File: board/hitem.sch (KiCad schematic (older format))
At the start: 44 parts, among them J1 Female, 0.1\", 1x10, J2 Female, 0.1\", 1x10, J3 Header, .100\", J4 CONN_01X03, J5 Header, .100\", J6 CONN_01X01, J7 CONN_01X01, Q1 BSS214N, Q2 BSS214N, Q3 BSS214N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

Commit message: Fix incorrect footprint for U2
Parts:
- U2: footprint hitem:XC6221 -> hitem:SSOT-24
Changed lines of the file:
@@
 $EndComp
 $Comp
-L GND #PWR16
+L GND #PWR01
 U 1 1 56BBA380
 P 9350 4450
-F 0 "#PWR16" H 9350 4200 50  0001 C CNN
+F 0 "#PWR01" H 9350 4200 50  0001 C CNN
 F 1 "GND" H 9350 4300 50  0000 C CNN
 F 2 "" H 9350 4450 50  0000 C CNN
@@
 $EndComp
 $Comp
-L +BATT #PWR17
+L +BATT #PWR02
 U 1 1 56BD2B63
 P 9600 3500
-F 0 "#PWR17" H 9600 3350 50  0001 C CNN
+F 0 "#PWR02" H 9600 3350 50  0001 C CNN
 F 1 "+BATT" H 9600 3640 50  0000 C CNN
 F 2 "" H 9600 3500 50  0000 C CNN
@@
 $EndComp
 $Comp
-L GND #PWR2
+L GND #PWR03
 U 1 1 56BDEC0D
 P 1300 2450
-F 0 "#PWR2" H 1300 2200 50  0001 C CNN
+F 0 "#PWR03" H 1300 2200 50  0001 C CNN
 F 1 "GND" H 1300 2300 50  0000 C CNN
 F 2 "" H 1300 2450 50  0000 C CNN
@@
 $EndComp
 $Comp
-L +BATT #PWR12
+L +BATT #PWR04
 U 1 1 56BE7511
 P 6550 6350
-F 0 "#PWR12" H 6550 6200 50  0001 C CNN
+F 0 "#PWR04" H 6550 6200 50  0001 C CNN
 F 1 "+BATT" H 6550 6490 50  0000 C CNN
 F 2 "" H 6550 6350 50  0000 C CNN
@@
 Accelerometer
 $Comp
-L +BATT #PWR15
+L +BATT #PWR05
 U 1 1 56BFC041
 P 7650 2100
-F 0 "#PWR15" H 7650 1950 50  0001 C CNN
+F 0 "#PWR05" H 7650 1950 50  0001 C CNN
 F 1 "+BATT" H 7650 2240 50  0000 C CNN
 F 2 "" H 7650 2100 50  0000 C CNN
@@
 $EndComp
 $Comp
-L GND #PWR14
+L GND #PWR06
 U 1 1 56BFC2B6
 P 7250 2200
-F 0 "#PWR14" H 7250 1950 50  0001 C CNN
+F 0 "#PWR06" H 7250 1950 50  0001 C CNN
 F 1 "GND" H 7250 2050 50  0000 C CNN
 F 2 "" H 7250 2200 50  0000 C CNN
@@
 RedBearLab WiFi Micro
 $Comp
-L GND #PWR13
+L GND #PWR07
 U 1 1 56C2A2A1
 P 6550 7600
-F 0 "#PWR13" H 6550 7350 50  0001 C CNN
+F 0 "#PWR07" H 6550 7350 50  0001 C CNN
 F 1 "GND" H 6550 7450 50  0000 C CNN
 F 2 "" H 6550 7600 50  0000 C CNN
@@
 $EndComp
 $Comp
-L GND #PWR9
+L GND #PWR08
 U 1 1 58815443
 P 5200 7550
-F 0 "#PWR9" H 5200 7300 50  0001 C CNN
+F 0 "#PWR08" H 5200 7300 50  0001 C CNN
 F 1 "GND" H 5200 7400 50  0000 C CNN
 F 2 "" H 5200 7550 50  0000 C CNN
@@
 $EndComp
 $Comp
-L +BATT #PWR8
+L +BATT #PWR09
 U 1 1 58815930
 P 4450 6300
-F 0 "#PWR8" H 4450 6150 50  0001 C CNN
+F 0 "#PWR09" H 4450 6150 50  0001 C CNN
 F 1 "+BATT" H 4450 6440 50  0000 C CNN
 F 2 "" H 4450 6300 50  0000 C CNN
@@
 BATT-
 $Comp
-L +3.3V #PWR10
+L +3.3V #PWR010
 U 1 1 588160AF
 P 5800 6300
-F 0 "#PWR10" H 5800 6150 50  0001 C CNN
+F 0 "#PWR010" H 5800 6150 50  0001 C CNN
 F 1 "+3.3V" H 5800 6440 50  0000 C CNN
 F 2 "" H 5800 6300 50  0000 C CNN
@@
 F 0 "U2" H 2700 7150 60  0000 C CNN
 F 1 "XC6120" H 2800 7050 60  0000 C CNN
-F 2 "hitem:XC6221" H 2900 6850 60  0001 C CNN
+F 2 "hitem:SSOT-24" H 2900 6850 60  0001 C CNN
 F 3 "" H 2900 6850 60  0001 C CNN
 	1    2900 6850
@@
 $EndComp
 $Comp
-L +3.3V #PWR1
+L +3.3V #PWR011
 U 1 1 588219D9
 P 1300 800
-F 0 "#PWR1" H 1300 650 50  0001 C CNN
+F 0 "#PWR011" H 1300 650 50  0001 C CNN
 F 1 "+3.3V" H 1300 940 50  0000 C CNN
 F 2 "" H 1300 800 50  0000 C CNN
@@
 $EndComp
 $Comp
-L GND #PWR4
+L GND #PWR012
 U 1 1 588224EC
 P 2900 2450
-F 0 "#PWR4" H 2900 2200 50  0001 C CNN
+F 0 "#PWR012" H 2900 2200 50  0001 C CNN
 F 1 "GND" H 2900 2300 50  0000 C CNN
 F 2 "" H 2900 2450 50  0000 C CNN
@@
 $EndComp
 $Comp
-L +3.3V #PWR7
+L +3.3V #PWR013
 U 1 1 58822845
 P 4050 1450
-F 0 "#PWR7" H 4050 1300 50  0001 C CNN
+F 0 "#PWR013" H 4050 1300 50  0001 C CNN
 F 1 "+3.3V" V 4050 1700 50  0000 C CNN
 F 2 "" H 4050 1450 50  0000 C CNN
@@
 $EndComp
 $Comp
-L GND #PWR6
+L GND #PWR014
 U 1 1 58823532
 P 3600 1550
-F 0 "#PWR6" H 3600 1300 50  0001 C CNN
+F 0 "#PWR014" H 3600 1300 50  0001 C CNN
 F 1 "GND" H 3600 1400 50  0000 C CNN
 F 2 "" H 3600 1550 50  0000 C CNN
@@
 $EndComp
 $Comp
-L GND #PWR11
+L GND #PWR015
 U 1 1 588235D0
 P 6100 1500
-F 0 "#PWR11" H 6100 1250 50  0001 C CNN
+F 0 "#PWR015" H 6100 1250 50  0001 C CNN
 F 1 "GND" H 6100 1350 50  0000 C CNN
 F 2 "" H 6100 1500 50  0000 C CNN
@@
 $EndComp
 $Comp
-L GND #PWR5
+L GND #PWR016
 U 1 1 5897CAC5
 P 2950 5150
-F 0 "#PWR5" H 2950 4900 50  0001 C CNN
+F 0 "#PWR016" H 2950 4900 50  0001 C CNN
 F 1 "GND" H 2950 5000 50  0000 C CNN
 F 2 "" H 2950 5150 50  0000 C CNN
@@
 $EndComp
 $Comp
-L +BATT #PWR3
+L +BATT #PWR017
 U 1 1 5897E7A3
 P 2650 3800
-F 0 "#PWR3" H 2650 3650 50  0001 C CNN
+F 0 "#PWR017" H 2650 3650 50  0001 C CNN
 F 1 "+BATT" H 2650 3940 50  0000 C CNN
 F 2 "" H 2650 3800 50  0000 C CNN
@@
 AUX3
 $Comp
-L +3.3V #PWR19
+L +3.3V #PWR018
 U 1 1 58990CBB
 P 9800 3350
-F 0 "#PWR19" H 9800 3200 50  0001 C CNN
+F 0 "#PWR018" H 9800 3200 50  0001 C CNN
 F 1 "+3.3V" H 9800 3500 50  0000 C CNN
 F 2 "" H 9800 3350 50  0000 C CNN
@@
 	8550 5600 8550 3000
 $Comp
-L GND #PWR18
+L GND #PWR019
 U 1 1 58993345
 P 9650 5400
-F 0 "#PWR18" H 9650 5150 50  0001 C CNN
+F 0 "#PWR019" H 9650 5150 50  0001 C CNN
 F 1 "GND" H 9650 5250 50  0000 C CNN
 F 2 "" H 9650 5400 50  0000 C CNN

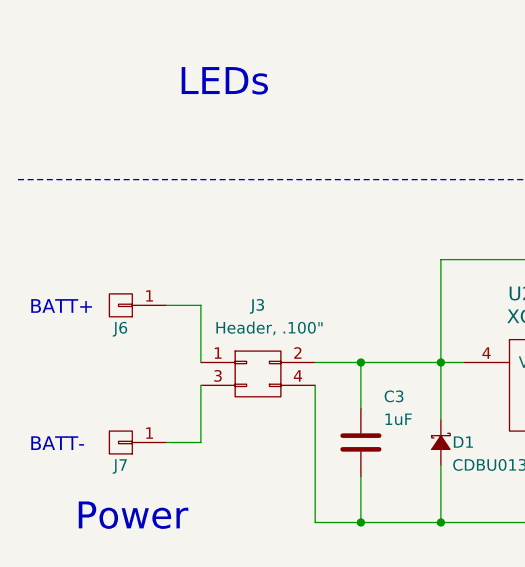
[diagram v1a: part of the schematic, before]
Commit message: Add protection Polyfuse
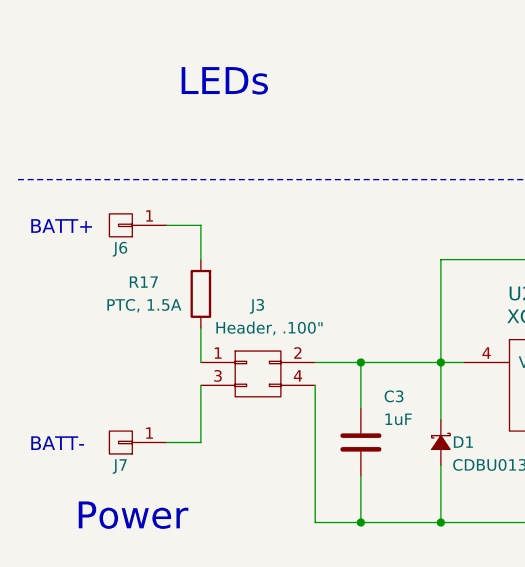
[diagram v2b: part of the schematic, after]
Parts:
- added R17: PTC, 1.5A, hitem:BEL-0ZCK, symbol R
- J1, J2: MANUFACTURER (none) -> Wurth Electronics; MOUSER (none) -> 710-61301011821; PART_NUMBER (none) -> 61301011821
- U1: MANUFACTURER (none) -> STMicroelectronics; MOUSER (none) -> 511-LIS3DHTR; PART_NUMBER (none) -> LIS3DHTR
- U2: MANUFACTURER (none) -> TOREX; MOUSER (none) -> 865-XC6120C302NR-G; PART_NUMBER (none) -> XC6120C302NR-G
- U6: MANUFACTURER (none) -> MICREL; MOUSER (none) -> 998-MIC5255-3.3YM5TR; PART_NUMBER (none) -> MIC5255-3.3YM5-TR
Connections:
- wire segments 165 -> 166
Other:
- moved on the sheet: J6
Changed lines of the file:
@@
 $EndComp
 $Comp
-L GND #PWR01
+L GND #PWR16
 U 1 1 56BBA380
 P 9350 4450
-F 0 "#PWR01" H 9350 4200 50  0001 C CNN
+F 0 "#PWR16" H 9350 4200 50  0001 C CNN
 F 1 "GND" H 9350 4300 50  0000 C CNN
 F 2 "" H 9350 4450 50  0000 C CNN
@@
 $EndComp
 $Comp
-L +BATT #PWR02
+L +BATT #PWR17
 U 1 1 56BD2B63
 P 9600 3500
-F 0 "#PWR02" H 9600 3350 50  0001 C CNN
+F 0 "#PWR17" H 9600 3350 50  0001 C CNN
 F 1 "+BATT" H 9600 3640 50  0000 C CNN
 F 2 "" H 9600 3500 50  0000 C CNN
@@
 $EndComp
 $Comp
-L GND #PWR03
+L GND #PWR2
 U 1 1 56BDEC0D
 P 1300 2450
-F 0 "#PWR03" H 1300 2200 50  0001 C CNN
+F 0 "#PWR2" H 1300 2200 50  0001 C CNN
 F 1 "GND" H 1300 2300 50  0000 C CNN
 F 2 "" H 1300 2450 50  0000 C CNN
@@
 $EndComp
 $Comp
-L +BATT #PWR04
+L +BATT #PWR12
 U 1 1 56BE7511
 P 6550 6350
-F 0 "#PWR04" H 6550 6200 50  0001 C CNN
+F 0 "#PWR12" H 6550 6200 50  0001 C CNN
 F 1 "+BATT" H 6550 6490 50  0000 C CNN
 F 2 "" H 6550 6350 50  0000 C CNN
@@
 Accelerometer
 $Comp
-L +BATT #PWR05
+L +BATT #PWR15
 U 1 1 56BFC041
 P 7650 2100
-F 0 "#PWR05" H 7650 1950 50  0001 C CNN
+F 0 "#PWR15" H 7650 1950 50  0001 C CNN
 F 1 "+BATT" H 7650 2240 50  0000 C CNN
 F 2 "" H 7650 2100 50  0000 C CNN
@@
 $EndComp
 $Comp
-L GND #PWR06
+L GND #PWR14
 U 1 1 56BFC2B6
 P 7250 2200
-F 0 "#PWR06" H 7250 1950 50  0001 C CNN
+F 0 "#PWR14" H 7250 1950 50  0001 C CNN
 F 1 "GND" H 7250 2050 50  0000 C CNN
 F 2 "" H 7250 2200 50  0000 C CNN
@@
 F 2 "Pin_Headers:Pin_Header_Straight_1x10" H 8100 1650 50  0001 C CNN
 F 3 "" H 8100 1650 50  0000 C CNN
+F 4 "710-61301011821" H 8100 1650 60  0001 C CNN "MOUSER"
+F 5 "61301011821" H 8100 1650 60  0001 C CNN "PART_NUMBER"
+F 6 "Wurth Electronics" H 8100 1650 60  0001 C CNN "MANUFACTURER"
 	1    8100 1650
 	1    0    0    -1
@@
 F 2 "Pin_Headers:Pin_Header_Straight_1x10" H 9750 1650 50  0001 C CNN
 F 3 "" H 9750 1650 50  0000 C CNN
+F 4 "710-61301011821" H 9750 1650 60  0001 C CNN "MOUSER"
+F 5 "61301011821" H 9750 1650 60  0001 C CNN "PART_NUMBER"
+F 6 "Wurth Electronics" H 9750 1650 60  0001 C CNN "MANUFACTURER"
 	1    9750 1650
 	-1   0    0    -1
@@
 RedBearLab WiFi Micro
 $Comp
-L GND #PWR07
+L GND #PWR13
 U 1 1 56C2A2A1
 P 6550 7600
-F 0 "#PWR07" H 6550 7350 50  0001 C CNN
+F 0 "#PWR13" H 6550 7350 50  0001 C CNN
 F 1 "GND" H 6550 7450 50  0000 C CNN
 F 2 "" H 6550 7600 50  0000 C CNN
@@
 L CONN_01X01 J6
 U 1 1 588141B5
-P 950 6600
-F 0 "J6" H 950 6700 50  0000 C CNN
-F 1 "CONN_01X01" V 1050 6600 50  0001 C CNN
-F 2 "hitem:BATTERY_CONTACT" H 950 6600 50  0001 C CNN
-F 3 "" H 950 6600 50  0000 C CNN
-	1    950  6600
+P 950 6250
+F 0 "J6" H 950 6350 50  0000 C CNN
+F 1 "CONN_01X01" V 1050 6250 50  0001 C CNN
+F 2 "hitem:BATTERY_CONTACT" H 950 6250 50  0001 C CNN
+F 3 "" H 950 6250 50  0000 C CNN
+	1    950  6250
 	-1   0    0    1
 $EndComp
@@
 $EndComp
 $Comp
-L GND #PWR08
+L GND #PWR9
 U 1 1 58815443
 P 5200 7550
-F 0 "#PWR08" H 5200 7300 50  0001 C CNN
+F 0 "#PWR9" H 5200 7300 50  0001 C CNN
 F 1 "GND" H 5200 7400 50  0000 C CNN
 F 2 "" H 5200 7550 50  0000 C CNN
@@
 $EndComp
 $Comp
-L +BATT #PWR09
+L +BATT #PWR8
 U 1 1 58815930
 P 4450 6300
-F 0 "#PWR09" H 4450 6150 50  0001 C CNN
+F 0 "#PWR8" H 4450 6150 50  0001 C CNN
 F 1 "+BATT" H 4450 6440 50  0000 C CNN
 F 2 "" H 4450 6300 50  0000 C CNN
@@
 	1    0    0    -1
 $EndComp
-Text Notes 550  6650 0    60   ~ 0
+Text Notes 550  6300 0    60   ~ 0
 BATT+
 Text Notes 550  7250 0    60   ~ 0
 BATT-
 $Comp
-L +3.3V #PWR010
+L +3.3V #PWR10
 U 1 1 588160AF
 P 5800 6300
-F 0 "#PWR010" H 5800 6150 50  0001 C CNN
+F 0 "#PWR10" H 5800 6150 50  0001 C CNN
 F 1 "+3.3V" H 5800 6440 50  0000 C CNN
 F 2 "" H 5800 6300 50  0000 C CNN
@@
 F 2 "hitem:SSOT-24" H 2900 6850 60  0001 C CNN
 F 3 "" H 2900 6850 60  0001 C CNN
+F 4 "865-XC6120C302NR-G" H 2900 6850 60  0001 C CNN "MOUSER"
+F 5 "XC6120C302NR-G" H 2900 6850 60  0001 C CNN "PART_NUMBER"
+F 6 "TOREX" H 2900 6850 60  0001 C CNN "MANUFACTURER"
 	1    2900 6850
 	1    0    0    -1
@@
 F 2 "hitem:LIS3DH" H 1900 1600 60  0001 C CNN
 F 3 "" H 1900 1600 60  0001 C CNN
+F 4 "511-LIS3DHTR" H 1900 1600 60  0001 C CNN "MOUSER"
+F 5 "LIS3DHTR" H 1900 1600 60  0001 C CNN "PART_NUMBER"
+F 6 "STMicroelectronics" H 1900 1600 60  0001 C CNN "MANUFACTURER"
 	1    1900 1600
 	1    0    0    -1
@@
 F 2 "hitem:MIC5255" H 5200 6450 60  0001 C CNN
 F 3 "" H 5200 6450 60  0001 C CNN
+F 4 "998-MIC5255-3.3YM5TR" H 5200 6450 60  0001 C CNN "MOUSER"
+F 5 "MIC5255-3.3YM5-TR" H 5200 6450 60  0001 C CNN "PART_NUMBER"
+F 6 "MICREL" H 5200 6450 60  0001 C CNN "MANUFACTURER"
 	1    5200 6450
 	1    0    0    -1
@@
 $EndComp
 $Comp
-L +3.3V #PWR011
+L +3.3V #PWR1
 U 1 1 588219D9
 P 1300 800
-F 0 "#PWR011" H 1300 650 50  0001 C CNN
+F 0 "#PWR1" H 1300 650 50  0001 C CNN
 F 1 "+3.3V" H 1300 940 50  0000 C CNN
 F 2 "" H 1300 800 50  0000 C CNN
@@
 $EndComp
 $Comp
-L GND #PWR012
+L GND #PWR4
 U 1 1 588224EC
 P 2900 2450
-F 0 "#PWR012" H 2900 2200 50  0001 C CNN
+F 0 "#PWR4" H 2900 2200 50  0001 C CNN
 F 1 "GND" H 2900 2300 50  0000 C CNN
 F 2 "" H 2900 2450 50  0000 C CNN
@@
 $EndComp
 $Comp
-L +3.3V #PWR013
+L +3.3V #PWR7
 U 1 1 58822845
 P 4050 1450
-F 0 "#PWR013" H 4050 1300 50  0001 C CNN
+F 0 "#PWR7" H 4050 1300 50  0001 C CNN
 F 1 "+3.3V" V 4050 1700 50  0000 C CNN
 F 2 "" H 4050 1450 50  0000 C CNN
@@
 $EndComp
 $Comp
-L GND #PWR014
+L GND #PWR6
 U 1 1 58823532
 P 3600 1550
-F 0 "#PWR014" H 3600 1300 50  0001 C CNN
+F 0 "#PWR6" H 3600 1300 50  0001 C CNN
 F 1 "GND" H 3600 1400 50  0000 C CNN
 F 2 "" H 3600 1550 50  0000 C CNN
@@
 $EndComp
 $Comp
-L GND #PWR015
+L GND #PWR11
 U 1 1 588235D0
 P 6100 1500
-F 0 "#PWR015" H 6100 1250 50  0001 C CNN
+F 0 "#PWR11" H 6100 1250 50  0001 C CNN
 F 1 "GND" H 6100 1350 50  0000 C CNN
 F 2 "" H 6100 1500 50  0000 C CNN
@@
 $EndComp
 $Comp
-L GND #PWR016
+L GND #PWR5
 U 1 1 5897CAC5
 P 2950 5150
-F 0 "#PWR016" H 2950 4900 50  0001 C CNN
+F 0 "#PWR5" H 2950 4900 50  0001 C CNN
 F 1 "GND" H 2950 5000 50  0000 C CNN
 F 2 "" H 2950 5150 50  0000 C CNN
@@
 $EndComp
 $Comp
-L +BATT #PWR017
+L +BATT #PWR3
 U 1 1 5897E7A3
 P 2650 3800
-F 0 "#PWR017" H 2650 3650 50  0001 C CNN
+F 0 "#PWR3" H 2650 3650 50  0001 C CNN
 F 1 "+BATT" H 2650 3940 50  0000 C CNN
 F 2 "" H 2650 3800 50  0000 C CNN
@@
 	6550 6400 6550 6350
 Wire Wire Line
-	1150 6600 1300 6600
-Wire Wire Line
-	1300 6600 1300 6850
+	1150 6250 1300 6250
 Wire Wire Line
 	1150 7200 1300 7200
@@
 AUX3
 $Comp
-L +3.3V #PWR018
+L +3.3V #PWR19
 U 1 1 58990CBB
 P 9800 3350
-F 0 "#PWR018" H 9800 3200 50  0001 C CNN
+F 0 "#PWR19" H 9800 3200 50  0001 C CNN
 F 1 "+3.3V" H 9800 3500 50  0000 C CNN
 F 2 "" H 9800 3350 50  0000 C CNN
@@
 	8550 5600 8550 3000
 $Comp
-L GND #PWR019
+L GND #PWR18
 U 1 1 58993345
 P 9650 5400
-F 0 "#PWR019" H 9650 5150 50  0001 C CNN
+F 0 "#PWR18" H 9650 5150 50  0001 C CNN
 F 1 "GND" H 9650 5250 50  0000 C CNN
 F 2 "" H 9650 5400 50  0000 C CNN
@@
 	6550 7550 6300 7550
 Connection ~ 6550 7550
+$Comp
+L R R17
+U 1 1 58A618BB
+P 1300 6550
+F 0 "R17" H 1550 6500 50  0000 C CNN
+F 1 "PTC, 1.5A" H 1550 6600 50  0000 C CNN
+F 2 "hitem:BEL-0ZCK" V 1230 6550 50  0001 C CNN
+F 3 "" H 1300 6550 50  0000 C CNN
+F 4 "530-0ZCK0075FF2E" H 1300 6550 60  0001 C CNN "MOUSER"
+F 5 "0ZCK0075FF2E" H 1300 6550 60  0001 C CNN "PART_NUMBET"
+F 6 "Bel Fuse" H 1300 6550 60  0001 C CNN "MANUFACTURER"
+	1    1300 6550
+	-1   0    0    1
+$EndComp
+Wire Wire Line
+	1300 6250 1300 6400
+Wire Wire Line
+	1300 6700 1300 6850
 $EndSCHEMATC
